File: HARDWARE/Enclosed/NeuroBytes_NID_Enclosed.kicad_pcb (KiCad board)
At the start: 2 copper layers, 40.6 x 72.2 mm, 65 parts, among them J1 CONN_01X05, J2 Conn_01x03, J3 USB_OTG, J4 Conn_01x03_Female, J5 Conn_01x03, J6 Conn_01x03_Female, J7 Conn_01x03, J8 Conn_01x03_Female, Q1 MMBT3904, Q2 2N7002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

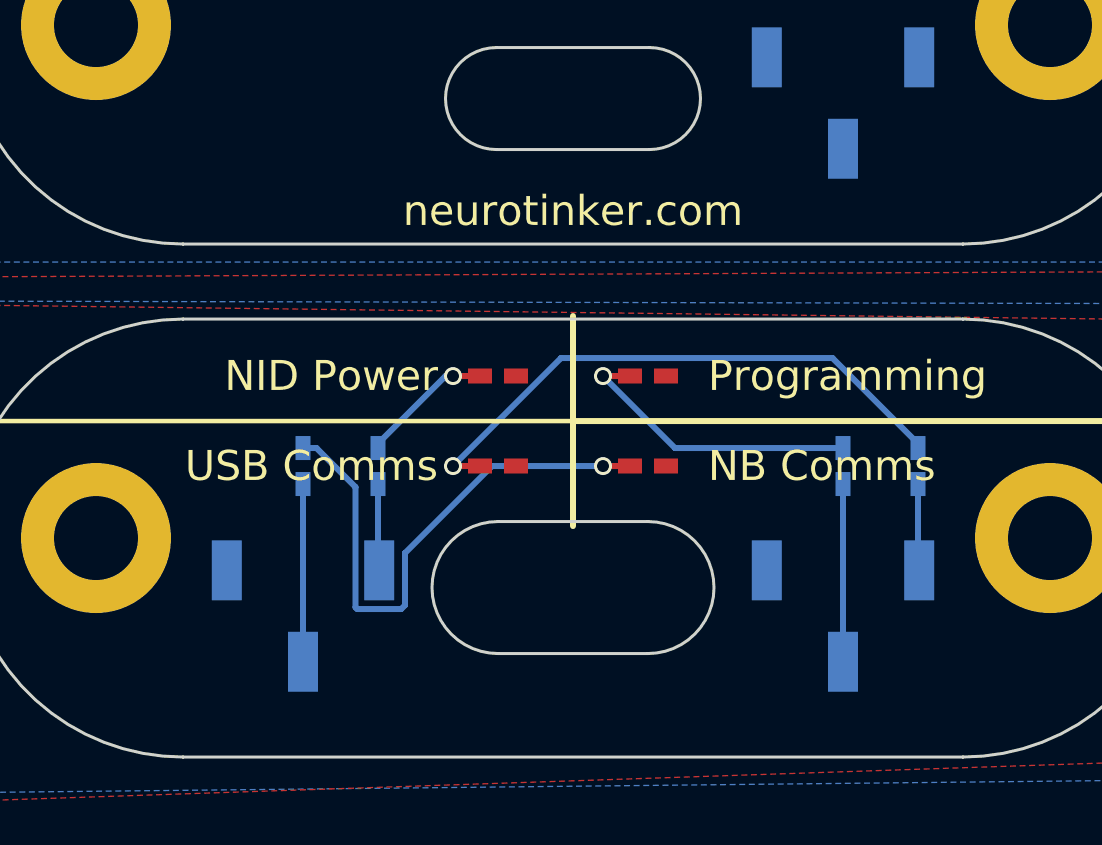
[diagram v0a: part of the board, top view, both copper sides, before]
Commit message: assembled and tested board; fixed reversed traces on front panel. front-only files only include this board so they can be ordered alone.
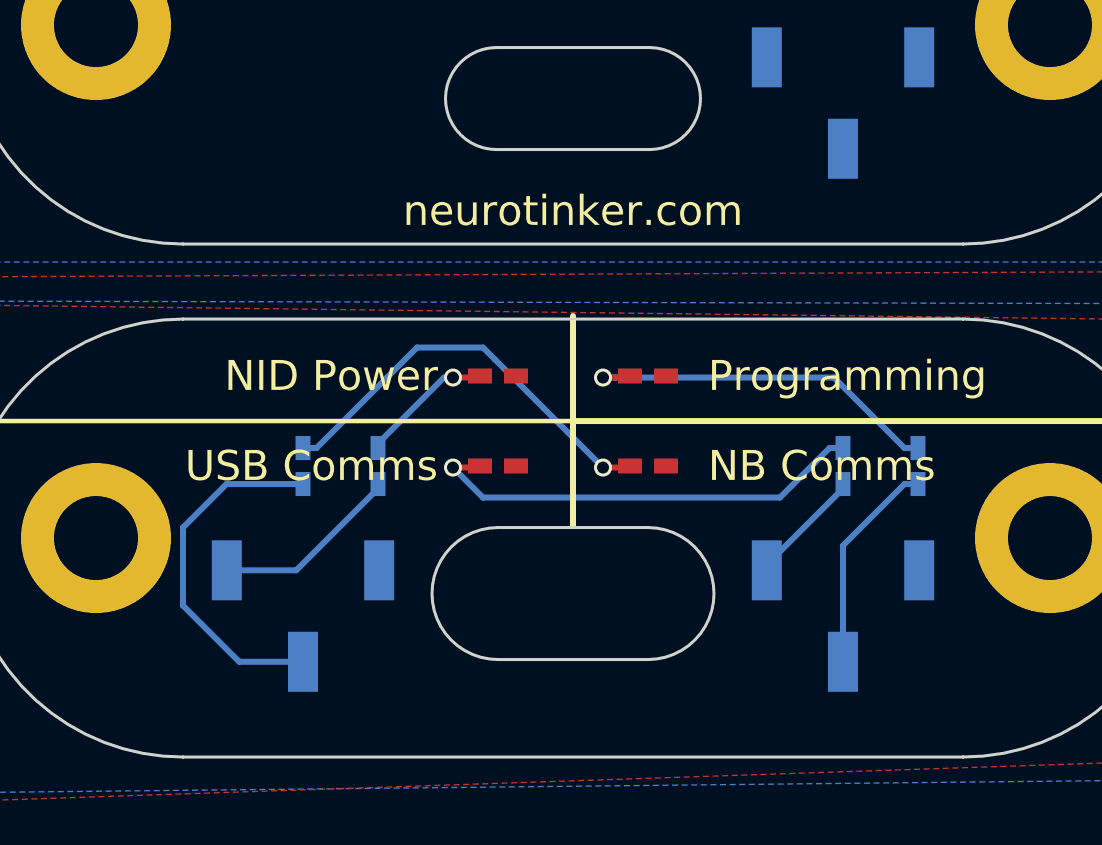
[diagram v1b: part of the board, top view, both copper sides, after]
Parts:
- moved R13 2.50 mm to (55.3, 107.5)
- moved R14 2.50 mm to (57.8, 107.5)
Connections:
- J1 pad : GND -> (no net)
- J4 pad 1: Net-(J4-Pad1) -> /GND_FRONT
- J4 pad 3: /GND_FRONT -> Net-(J4-Pad3)
- J6 pad 1: Net-(J6-Pad1) -> /GND_FRONT
- J6 pad 3: /GND_FRONT -> Net-(J6-Pad3)
- R11 pad 2: Net-(J4-Pad1) -> Net-(J4-Pad3)
- R13 pad 2: Net-(J6-Pad1) -> Net-(J6-Pad3)
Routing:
- net Net-(J4-Pad3): track 0.00 -> 6.32 mm
- net Net-(J4-Pad2): track 5.92 -> 12.0 mm
- net Net-(D2-Pad2): track 18.5 -> 14.0 mm
- net Net-(D3-Pad2): track 19.2 -> 15.0 mm
- net Net-(J6-Pad3): track 0.00 -> 3.93 mm
- net Net-(J6-Pad1): track 2.89 -> 0.00 mm
- net Net-(J4-Pad1): track 2.89 -> 0.00 mm
- net Net-(D4-Pad2): track 9.89 -> 12.4 mm
- net Net-(J6-Pad2): track 5.92 -> 7.22 mm
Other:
- outline, holes or cut-outs redrawn
